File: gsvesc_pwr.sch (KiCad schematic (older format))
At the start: 36 parts

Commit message: Aufgeräumt Teil 2
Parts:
- removed Q? (x4): IRF7749, Package_DirectFET:DirectFET_L6, symbol gsvec:IRF7749
- added Q? (x4): IRF7749, Package_DirectFET:DirectFET_L6, symbol gsvesc:IRF7749
- Q? (x2): symbol gsvec:IRF7749 -> gsvesc:IRF7749
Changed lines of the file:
@@
 $EndComp
 $Comp
-L gsvec:IRF7749 Q?
+L gsvesc:IRF7749 Q?
 U 1 1 5C06FA21
 P 2400 1750
+AR Path="/5C06FA21" Ref="Q?"  Part="1"
+AR Path="/5BECFABD/5C06FA21" Ref="Q?"  Part="1"
 F 0 "Q?" H 2606 1796 50  0000 L CNN
 F 1 "IRF7749" H 2606 1705 50  0000 L CNN
@@
 Motor Power
 $Comp
-L gsvec:IRF7749 Q?
+L gsvesc:IRF7749 Q?
 U 1 1 5BFF7141
 P 2400 2400
@@
 $EndComp
 $Comp
-L gsvec:IRF7749 Q?
-U 1 1 5BFFD587
-P 2400 4500
-F 0 "Q?" H 2606 4546 50  0000 L CNN
-F 1 "IRF7749" H 2606 4455 50  0000 L CNN
-F 2 "Package_DirectFET:DirectFET_L6" H 2400 4500 50  0001 C CIN
-F 3 "https://www.infineon.com/dgdl/irf6718l2pbf.pdf?fileId=5546d462533600a4015355ed25bd1a88" H 2400 4500 50  0001 L CNN
-	1    2400 4500
-	1    0    0    -1
-$EndComp
-$Comp
 L Device:R_Shunt R?
 U 1 1 5BFFD58D
@@
 $EndComp
 $Comp
-L gsvec:IRF7749 Q?
-U 1 1 5BFFD593
-P 2400 5150
-F 0 "Q?" H 2606 5196 50  0000 L CNN
-F 1 "IRF7749" H 2606 5105 50  0000 L CNN
-F 2 "Package_DirectFET:DirectFET_L6" H 2400 5150 50  0001 C CIN
-F 3 "https://www.infineon.com/dgdl/irf6718l2pbf.pdf?fileId=5546d462533600a4015355ed25bd1a88" H 2400 5150 50  0001 L CNN
-	1    2400 5150
-	1    0    0    -1
-$EndComp
-$Comp
 L Device:R R?
 U 1 1 5BFFD599
@@
 $EndComp
 $Comp
-L gsvec:IRF7749 Q?
-U 1 1 5BFFECDB
-P 6950 1750
-F 0 "Q?" H 7156 1796 50  0000 L CNN
-F 1 "IRF7749" H 7156 1705 50  0000 L CNN
-F 2 "Package_DirectFET:DirectFET_L6" H 6950 1750 50  0001 C CIN
-F 3 "https://www.infineon.com/dgdl/irf6718l2pbf.pdf?fileId=5546d462533600a4015355ed25bd1a88" H 6950 1750 50  0001 L CNN
-	1    6950 1750
-	1    0    0    -1
-$EndComp
-$Comp
 L Device:R_Shunt R?
 U 1 1 5BFFECE2
@@
 	1    8400 2050
 	0    1    1    0
-$EndComp
-$Comp
-L gsvec:IRF7749 Q?
-U 1 1 5BFFECE9
-P 6950 2400
-F 0 "Q?" H 7156 2446 50  0000 L CNN
-F 1 "IRF7749" H 7156 2355 50  0000 L CNN
-F 2 "Package_DirectFET:DirectFET_L6" H 6950 2400 50  0001 C CIN
-F 3 "https://www.infineon.com/dgdl/irf6718l2pbf.pdf?fileId=5546d462533600a4015355ed25bd1a88" H 6950 2400 50  0001 L CNN
-	1    6950 2400
-	1    0    0    -1
 $EndComp
 $Comp
@@
 Text HLabel 7550 5150 2    50   Input ~ 0
 TEMP
+$Comp
+L gsvesc:IRF7749 Q?
+U 1 1 5C01D073
+P 2400 4500
+F 0 "Q?" H 2606 4546 50  0000 L CNN
+F 1 "IRF7749" H 2606 4455 50  0000 L CNN
+F 2 "Package_DirectFET:DirectFET_L6" H 2400 4500 50  0001 C CIN
+F 3 "https://www.infineon.com/dgdl/irf6718l2pbf.pdf?fileId=5546d462533600a4015355ed25bd1a88" H 2400 4500 50  0001 L CNN
+	1    2400 4500
+	1    0    0    -1
+$EndComp
+$Comp
+L gsvesc:IRF7749 Q?
+U 1 1 5C01D10F
+P 2400 5150
+F 0 "Q?" H 2606 5196 50  0000 L CNN
+F 1 "IRF7749" H 2606 5105 50  0000 L CNN
+F 2 "Package_DirectFET:DirectFET_L6" H 2400 5150 50  0001 C CIN
+F 3 "https://www.infineon.com/dgdl/irf6718l2pbf.pdf?fileId=5546d462533600a4015355ed25bd1a88" H 2400 5150 50  0001 L CNN
+	1    2400 5150
+	1    0    0    -1
+$EndComp
+$Comp
+L gsvesc:IRF7749 Q?
+U 1 1 5C01D183
+P 6950 1750
+F 0 "Q?" H 7156 1796 50  0000 L CNN
+F 1 "IRF7749" H 7156 1705 50  0000 L CNN
+F 2 "Package_DirectFET:DirectFET_L6" H 6950 1750 50  0001 C CIN
+F 3 "https://www.infineon.com/dgdl/irf6718l2pbf.pdf?fileId=5546d462533600a4015355ed25bd1a88" H 6950 1750 50  0001 L CNN
+	1    6950 1750
+	1    0    0    -1
+$EndComp
+$Comp
+L gsvesc:IRF7749 Q?
+U 1 1 5C01D23F
+P 6950 2400
+F 0 "Q?" H 7156 2446 50  0000 L CNN
+F 1 "IRF7749" H 7156 2355 50  0000 L CNN
+F 2 "Package_DirectFET:DirectFET_L6" H 6950 2400 50  0001 C CIN
+F 3 "https://www.infineon.com/dgdl/irf6718l2pbf.pdf?fileId=5546d462533600a4015355ed25bd1a88" H 6950 2400 50  0001 L CNN
+	1    6950 2400
+	1    0    0    -1
+$EndComp
 $EndSCHEMATC

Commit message: SCM Fertig
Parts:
- removed C? (x3): C, symbol Device:C
- removed Q? (x6): IRF7749, Package_DirectFET:DirectFET_L6, symbol gsvesc:IRF7749
- removed R? (x3): R_Shunt, symbol Device:R_Shunt
- added C39, C42, C44: 10u0/16V, Capacitor_SMD:C_0805_2012Metric, symbol Device:C
- added Q1, Q2, Q3, Q4, Q5, Q6: NVMFS5C604, gsvesc:DFN500X600X110-5N, symbol gsvesc:NVMFS5C604
- added R31, R32, R37: 0R0005, Resistor_SMD:R_2512_6332Metric, symbol Device:R
- C35, C40, C41: renamed from C?; footprint (none) -> Capacitor_SMD:C_0805_2012Metric
- C36, C37, C43: renamed from C?; value 47u0 100V -> 47u0/100V; footprint (none) -> Capacitor_SMD:C_1210_3225Metric
- C38: renamed from C?; value C -> 10u0/16V; footprint (none) -> Capacitor_SMD:C_0805_2012Metric
- J10, J11, J13: renamed from J?; footprint (none) -> Connector_Wire:SolderWirePad_1x01_Drill2.5mm
- J12: renamed from J?; footprint (none) -> Connector_PinHeader_2.54mm:PinHeader_2x01_P2.54mm_Vertical
- R25, R26, R27, R28, R29, R30, R33, R34, R35: renamed from R?; footprint (none) -> Resistor_SMD:R_0805_2012Metric
- R36: renamed from R?; value R -> 10K0; footprint (none) -> Resistor_SMD:R_0805_2012Metric
- U4, U5, U6: renamed from U?; footprint (none) -> Package_SO:MSOP-8_3x3mm_P0.65mm
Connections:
- wire segments 130 -> 124

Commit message: design finished gerber created
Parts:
- J10: value PHASE_A -> PHASE_C; footprint Connector_Wire:SolderWirePad_1x01_Drill2.5mm -> Connector_Wire:SolderWirePad_1x01_SMD_5x10mm
- J11: value PHASE_C -> PHASE_A; footprint Connector_Wire:SolderWirePad_1x01_Drill2.5mm -> Connector_Wire:SolderWirePad_1x01_SMD_5x10mm
- J13: footprint Connector_Wire:SolderWirePad_1x01_Drill2.5mm -> Connector_Wire:SolderWirePad_1x01_SMD_5x10mm
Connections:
- net CURR_A: now also C41.1, R33.2; no longer C35.1, R29.2
- net CURR_C: now also C35.1, R29.2; no longer C41.1, R33.2
- net C_A: now also R33.1, U5.5 (OUT); no longer R29.1, U4.5 (OUT)
- net C_C: now also R29.1, U4.5 (OUT); no longer R33.1, U5.5 (OUT)
- net GH_A: now also R27.2; no longer R25.2
- net GH_C: now also R25.2; no longer R27.2
- net GL_A: now also R28.2; no longer R26.2
- net GL_C: now also R26.2; no longer R28.2
- net SH_A: now also Q3.3 (S), Q4.1 (D), R32.2, U5.8 (IN+); no longer Q1.3 (S), Q2.1 (D), R31.2, U4.8 (IN+)
- net SH_C: now also Q1.3 (S), Q2.1 (D), R31.2, U4.8 (IN+); no longer Q3.3 (S), Q4.1 (D), R32.2, U5.8 (IN+)
- net PHASE_C: now reaches J10.1 (Pin_1), R31.1, U4.1 (IN-)
- net PHASE_A: now reaches J11.1 (Pin_1), R32.1, U5.1 (IN-)
- net PHASE_B: now reaches J13.1 (Pin_1), R37.1, U6.1 (IN-)
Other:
- moved on the sheet: J10
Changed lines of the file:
@@
 L Connector_Generic:Conn_01x01 J10
 U 1 1 5BFF78B6
-P 4600 2050
-F 0 "J10" H 4680 2092 50  0000 L CNN
-F 1 "PHASE_A" H 4680 2001 50  0000 L CNN
-F 2 "Connector_Wire:SolderWirePad_1x01_Drill2.5mm" H 4600 2050 50  0001 C CNN
-F 3 "~" H 4600 2050 50  0001 C CNN
-	1    4600 2050
+P 4750 2050
+F 0 "J10" H 4830 2092 50  0000 L CNN
+F 1 "PHASE_C" H 4830 2001 50  0000 L CNN
+F 2 "Connector_Wire:SolderWirePad_1x01_SMD_5x10mm" H 4750 2050 50  0001 C CNN
+F 3 "~" H 4750 2050 50  0001 C CNN
+	1    4750 2050
 	1    0    0    -1
 $EndComp
@@
 	3000 1300 3000 1500
 Wire Wire Line
-	4050 2050 4400 2050
+	4050 2050 4550 2050
 Wire Wire Line
 	3450 2800 3300 2800
@@
 	4250 2700 4500 2700
 Text HLabel 1650 1750 0    50   Input ~ 0
-GH_A
+GH_C
 Text HLabel 1650 2400 0    50   Input ~ 0
-GL_A
+GL_C
 Wire Wire Line
 	1650 2400 1800 2400
@@
 	1650 2700 2500 2700
 Text HLabel 1650 2050 0    50   Input ~ 0
-SH_A
+SH_C
 Text HLabel 1650 2700 0    50   Input ~ 0
-SL_A
+SL_C
 Wire Wire Line
 	1650 2050 2500 2050
@@
 P 4600 4800
 F 0 "J11" H 4679 4842 50  0000 L CNN
-F 1 "PHASE_C" H 4679 4751 50  0000 L CNN
-F 2 "Connector_Wire:SolderWirePad_1x01_Drill2.5mm" H 4600 4800 50  0001 C CNN
+F 1 "PHASE_A" H 4679 4751 50  0000 L CNN
+F 2 "Connector_Wire:SolderWirePad_1x01_SMD_5x10mm" H 4600 4800 50  0001 C CNN
 F 3 "~" H 4600 4800 50  0001 C CNN
 	1    4600 4800
@@
 	4250 5450 4500 5450
 Text HLabel 1650 4500 0    50   Input ~ 0
-GH_C
+GH_A
 Text HLabel 1650 5150 0    50   Input ~ 0
-GL_C
+GL_A
 Wire Wire Line
 	1650 5150 1800 5150
@@
 	1650 5450 2500 5450
 Text HLabel 1650 4800 0    50   Input ~ 0
-SH_C
+SH_A
 Text HLabel 1650 5450 0    50   Input ~ 0
-SL_C
+SL_A
 Wire Wire Line
 	1650 4800 2500 4800
@@
 F 0 "J13" H 9229 2092 50  0000 L CNN
 F 1 "PHASE_B" H 9229 2001 50  0000 L CNN
-F 2 "Connector_Wire:SolderWirePad_1x01_Drill2.5mm" H 9150 2050 50  0001 C CNN
+F 2 "Connector_Wire:SolderWirePad_1x01_SMD_5x10mm" H 9150 2050 50  0001 C CNN
 F 3 "~" H 9150 2050 50  0001 C CNN
 	1    9150 2050
@@
 	2300 6750 2500 6750
 Text Label 4500 2700 0    50   ~ 0
-C_A
+C_C
 Text Label 9050 2700 0    50   ~ 0
 C_B
 Text Label 4500 5450 0    50   ~ 0
+C_A
+Text Label 2500 6750 0    50   ~ 0
 C_C
-Text Label 2500 6750 0    50   ~ 0
-C_A
 Wire Wire Line
 	1850 7150 1850 7300
@@
 $EndComp
 Text HLabel 1650 6750 0    50   Input ~ 0
-CURR_A
+CURR_C
 $Comp
 L Device:R R30
@@
 	5650 6750 5850 6750
 Text Label 5850 6750 0    50   ~ 0
-C_C
+C_A
 Wire Wire Line
 	5200 7150 5200 7300
@@
 $EndComp
 Text HLabel 5000 6750 0    50   Input ~ 0
-CURR_C
+CURR_A
 $Comp
 L Device:R R36
@@
 Wire Wire Line
 	8600 2050 8600 2300
+Text Label 4150 2050 0    50   ~ 0
+PHASE_C
+Text Label 8650 2050 0    50   ~ 0
+PHASE_B
+Text Label 4100 4800 0    50   ~ 0
+PHASE_A
 $EndSCHEMATC

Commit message: change inverter to npn :)
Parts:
- Q1, Q2, Q3, Q4, Q5, Q6: symbol gsvesc:NVMFS5C604 -> gsvesc-rescue:NVMFS5C604-gsvesc
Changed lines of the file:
@@
 TEMP
 $Comp
-L gsvesc:NVMFS5C604 Q1
+L gsvesc-rescue:NVMFS5C604-gsvesc Q1
 U 1 1 5C0115F0
 P 2400 1750
@@
 $EndComp
 $Comp
-L gsvesc:NVMFS5C604 Q2
+L gsvesc-rescue:NVMFS5C604-gsvesc Q2
 U 1 1 5C0116A7
 P 2400 2400
@@
 $EndComp
 $Comp
-L gsvesc:NVMFS5C604 Q3
+L gsvesc-rescue:NVMFS5C604-gsvesc Q3
 U 1 1 5C011719
 P 2400 4500
@@
 $EndComp
 $Comp
-L gsvesc:NVMFS5C604 Q4
+L gsvesc-rescue:NVMFS5C604-gsvesc Q4
 U 1 1 5C0117A7
 P 2400 5150
@@
 $EndComp
 $Comp
-L gsvesc:NVMFS5C604 Q5
+L gsvesc-rescue:NVMFS5C604-gsvesc Q5
 U 1 1 5C011819
 P 6950 1750
@@
 $EndComp
 $Comp
-L gsvesc:NVMFS5C604 Q6
+L gsvesc-rescue:NVMFS5C604-gsvesc Q6
 U 1 1 5C0118E7
 P 6950 2400

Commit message: test
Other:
- moved on the sheet: C35, C36, C37, C38, C39, C40, C41, C42, C43, C44, J10, J11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

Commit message: gsesc v3, work in progress
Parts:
- added C14, C24, C47: 1n00, Capacitor_SMD:C_0805_2012Metric, symbol Device:C
- added U7, U8, U9: M74VHC1GT66DTT1G, gsvesc:M74VHC1GT66DTT1G, symbol gsvesc:M74VHC1GT66DTT1G
- C35, C40, C41: value 4n70 -> 1n00
- C36, C37, C43: value 47u0/100V -> 10u0/100V
- J10, J11, J13: footprint Connector_Wire:SolderWirePad_1x01_SMD_5x10mm -> gsvesc:TestPoint_Pad_5.0x5.0mm
- Q1, Q2, Q3, Q4, Q5, Q6: symbol gsvesc-rescue:NVMFS5C604-gsvesc -> gsvesc:NVMFS5C604
- R29, R30, R33: value 100R -> 1k00
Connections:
- net CURR_A: now also C47.1, U9.1 (IO_XA); no longer C41.1
- net CURR_B: now also U8.1 (IO_XA)
- net CURR_C: now also U7.1 (IO_XA)
- net GND: now also C14.2, C24.2, C47.2, U7.3 (GND), U8.3 (GND), U9.3 (GND)
- net VCC: now also U7.5 (VCC), U8.5 (VCC), U9.5 (VCC)
- new net: C14.1, U7.2 (IO_YA)
- new net: C24.1, U8.2 (IO_YA)
- new net: C41.1, U9.2 (IO_YA)
- new net CURR_FILTER: U7.4 (ON/OFF), U8.4 (ON/OFF), U9.4 (ON/OFF)
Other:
- note added: "Place near to FETs"
- note removed: "Place with cable near to FETs"
- moved on the sheet: C35, C36, C37, C38, C39, C42, C43, C44, J10, J11, J12, J13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

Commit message: Update
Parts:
- C36, C37, C43: value 10u0/100V -> 10u0/75V
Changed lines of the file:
@@
 P 2200 1450
 F 0 "C36" H 2250 1550 50  0000 L CNN
-F 1 "10u0/100V" H 2250 1350 50  0000 L CNN
+F 1 "10u0/75V" H 2250 1350 50  0000 L CNN
 F 2 "Capacitor_SMD:C_1210_3225Metric" H 2238 1300 50  0001 C CNN
 F 3 "~" H 2200 1450 50  0001 C CNN
@@
 P 9350 1450
 F 0 "C37" H 9400 1550 50  0000 L CNN
-F 1 "10u0/100V" H 9400 1350 50  0000 L CNN
+F 1 "10u0/75V" H 9400 1350 50  0000 L CNN
 F 2 "Capacitor_SMD:C_1210_3225Metric" H 9388 1300 50  0001 C CNN
 F 3 "~" H 9350 1450 50  0001 C CNN
@@
 P 5700 1450
 F 0 "C43" H 5750 1550 50  0000 L CNN
-F 1 "10u0/100V" H 5750 1350 50  0000 L CNN
+F 1 "10u0/75V" H 5750 1350 50  0000 L CNN
 F 2 "Capacitor_SMD:C_1210_3225Metric" H 5738 1300 50  0001 C CNN
 F 3 "~" H 5700 1450 50  0001 C CNN

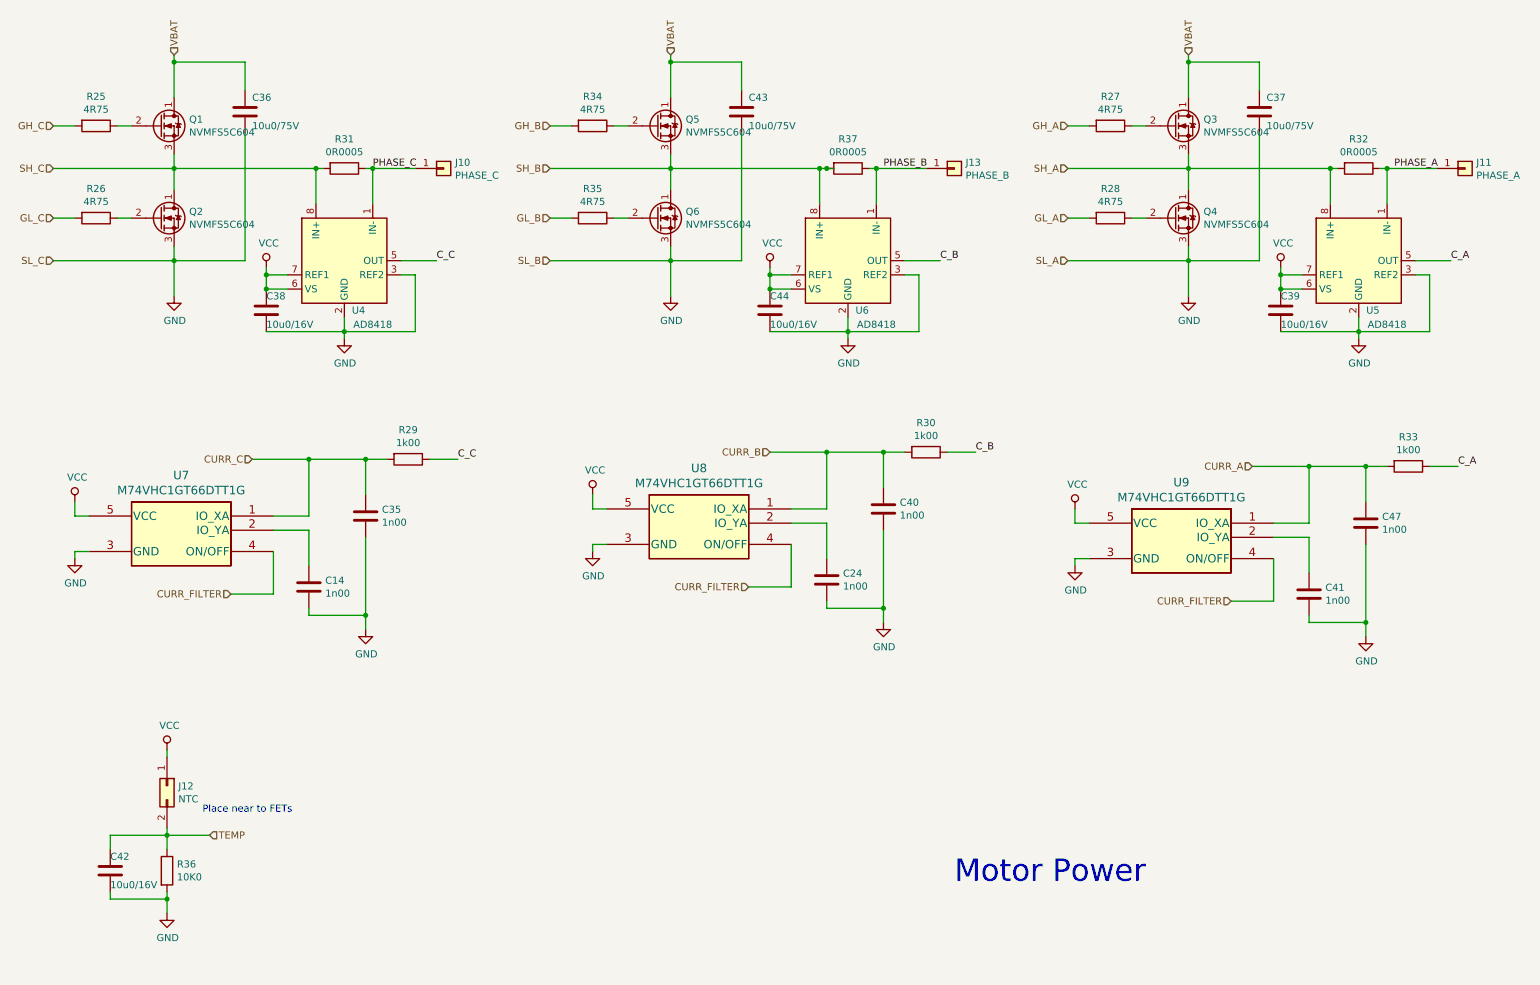
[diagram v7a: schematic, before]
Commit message: Umbau auf doppelFET, INA240
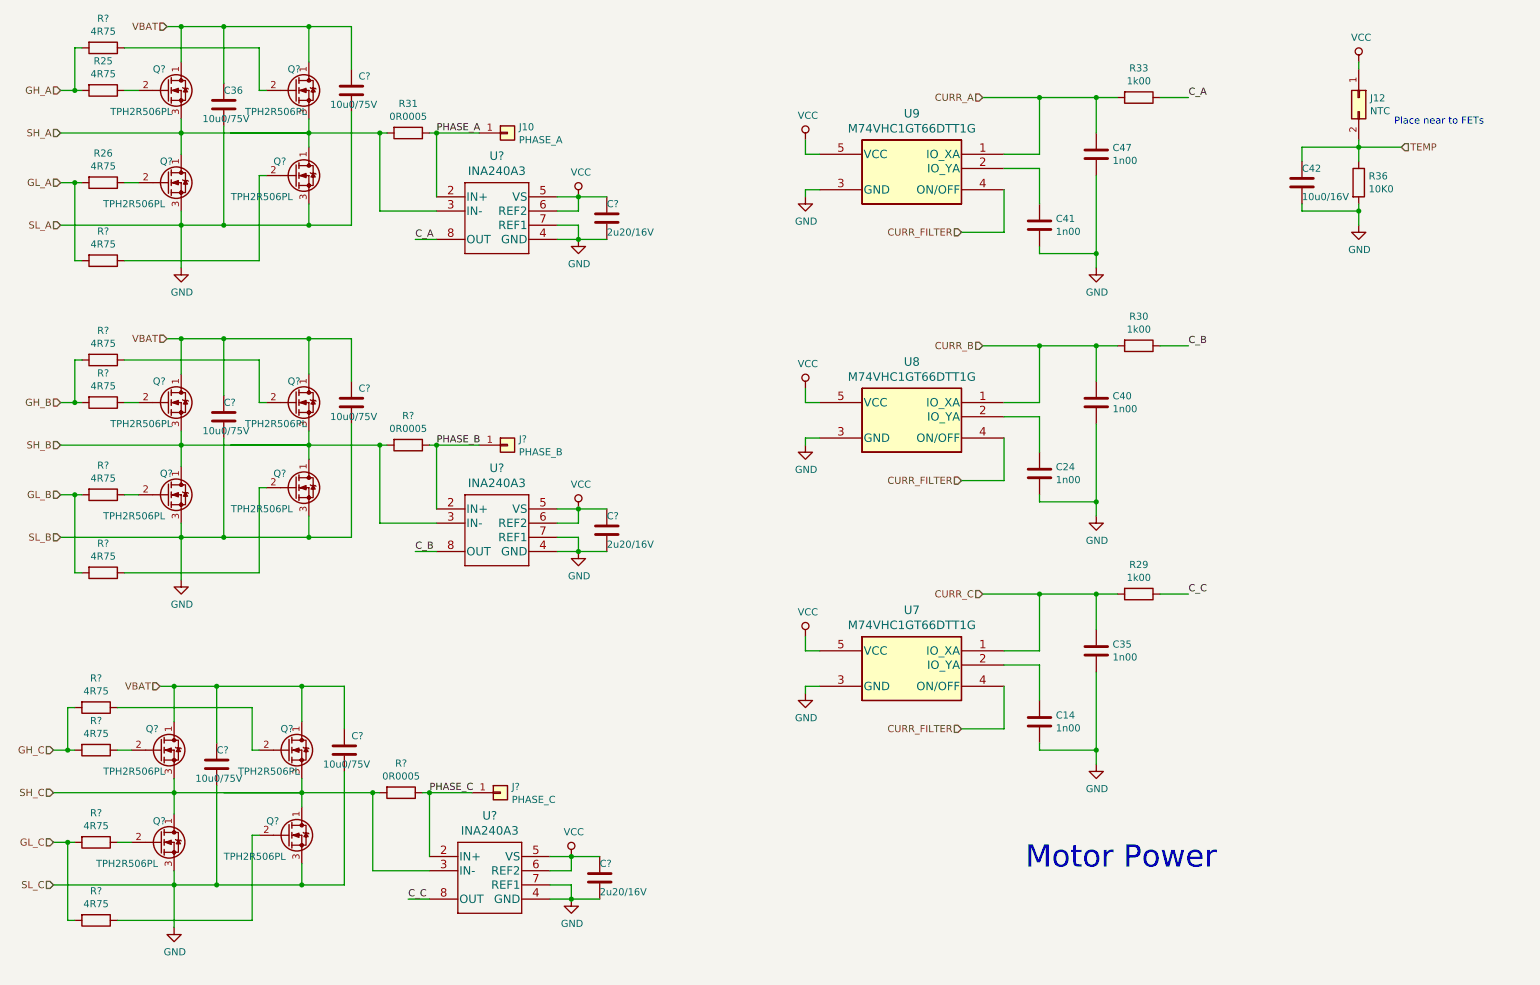
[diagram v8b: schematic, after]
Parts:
- removed C37, C43: 10u0/75V, Capacitor_SMD:C_1210_3225Metric, symbol Device:C
- removed C38, C39, C44: 10u0/16V, Capacitor_SMD:C_0805_2012Metric, symbol Device:C
- removed J11: PHASE_A, gsvesc:TestPoint_Pad_5.0x5.0mm, symbol Connector_Generic:Conn_01x01
- removed J13: PHASE_B, gsvesc:TestPoint_Pad_5.0x5.0mm, symbol Connector_Generic:Conn_01x01
- removed Q1, Q2, Q3, Q4, Q5, Q6: NVMFS5C604, gsvesc:DFN500X600X110-5N, symbol gsvesc:NVMFS5C604
- removed R27, R28, R34, R35: 4R75, Resistor_SMD:R_0805_2012Metric, symbol Device:R
- removed R32, R37: 0R0005, Resistor_SMD:R_2512_6332Metric, symbol Device:R
- removed U4, U5, U6: AD8418, Package_SO:MSOP-8_3x3mm_P0.65mm, symbol Amplifier_Current:AD8418
- added C? (x5): 10u0/75V, Capacitor_SMD:C_1210_3225Metric, symbol Device:C
- added C? (x3): 2u20/16V, Capacitor_SMD:C_0805_2012Metric, symbol Device:C
- added J?: PHASE_B, gsvesc:TestPoint_Pad_5.0x5.0mm, symbol Connector_Generic:Conn_01x01
- added J?: PHASE_C, gsvesc:TestPoint_Pad_5.0x5.0mm, symbol Connector_Generic:Conn_01x01
- added Q? (x12): TPH2R506PL, symbol gsvesc:TPH2R506PL
- added R? (x10): 4R75, Resistor_SMD:R_0805_2012Metric, symbol Device:R
- added R? (x2): 0R0005, Resistor_SMD:R_2512_6332Metric, symbol Device:R
- added U? (x3): INA240A3, PW0008A_N, symbol gsvesc:INA240A3
- J10: value PHASE_C -> PHASE_A
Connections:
- net C_A: now also U?.8 (OUT)
- net C_B: now also U?.8 (OUT)
- net C_C: now also U?.8 (OUT)
- net GH_A: now also R25.2, R?.2
- net GH_B: now also R?.2, R?.2
- net GH_C: now also R?.2, R?.2; no longer R25.2
- net GL_A: now also R26.2, R?.2
- net GL_B: now also R?.2, R?.2
- net GL_C: now also R?.2, R?.2; no longer R26.2
- net GND: now also C?.2, C?.2, C?.2, C?.2, C?.2, C?.2, C?.2, C?.2, Q?.3 (S), Q?.3 (S), Q?.3 (S), Q?.3 (S), Q?.3 (S), Q?.3 (S), U?.4 (GND), U?.4 (GND), U?.4 (GND), U?.7 (REF1), U?.7 (REF1), U?.7 (REF1)
- net PHASE_A: now also J10.1 (Pin_1), R31.1, U?.2 (IN+)
- net PHASE_B: now also J?.1 (Pin_1), R?.1, U?.2 (IN+)
- net PHASE_C: now also J?.1 (Pin_1), R?.1, U?.2 (IN+); no longer J10.1 (Pin_1), R31.1
- net SH_A: now also R31.2, Q?.1 (D), Q?.1 (D), Q?.3 (S), Q?.3 (S), U?.3 (IN-)
- net SH_B: now also Q?.1 (D), Q?.1 (D), Q?.3 (S), Q?.3 (S), R?.2, U?.3 (IN-)
- net SH_C: now also Q?.1 (D), Q?.1 (D), Q?.3 (S), Q?.3 (S), R?.2, U?.3 (IN-); no longer R31.2
- net VBAT: now also C?.1, C?.1, C?.1, C?.1, C?.1, Q?.1 (D), Q?.1 (D), Q?.1 (D), Q?.1 (D), Q?.1 (D), Q?.1 (D)
- net VCC: now also C?.1, C?.1, C?.1, U?.5 (VS), U?.5 (VS), U?.5 (VS), U?.6 (REF2), U?.6 (REF2), U?.6 (REF2)
- net at R26.1: now also Q?.2 (G)
- net at R25.1: now also Q?.2 (G)
- new net: Q?.2 (G), R?.1 (x10)
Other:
- moved on the sheet: C14, C24, C35, C36, C40, C41, C42, C47, J10, J12, R25, R26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
